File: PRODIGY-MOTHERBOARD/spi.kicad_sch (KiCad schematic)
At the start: 5 parts, among them U15 TXS0108EPW, U25 74HC138

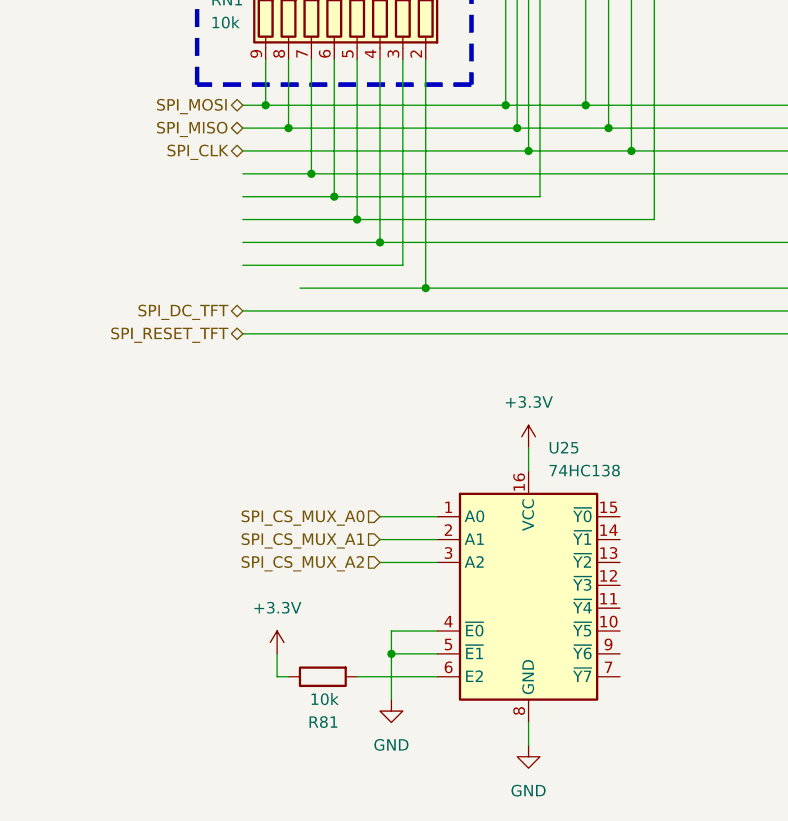
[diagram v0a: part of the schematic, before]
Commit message: Added proper debounce filter elements to buttons.
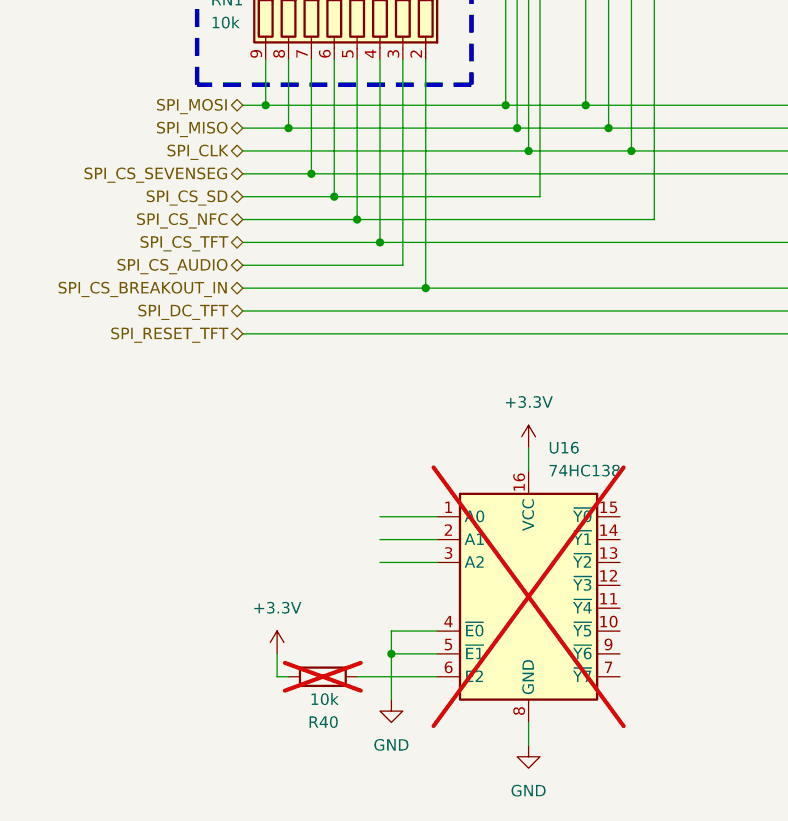
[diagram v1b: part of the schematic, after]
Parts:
- R40: renamed from R81; now not fitted
- U16: renamed from U25; now not fitted
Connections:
- net SPI_CS_SEVENSEG: now reaches RN1.7 (R6), U15.5 (A4)
- net SPI_CS_BREAKOUT_IN: now reaches RN1.2 (R1), U15.6 (A5)
- net SPI_CS_AUDIO: now reaches RN1.3 (R2)
- net CS_SD renamed SPI_CS_SD
- net NFC/SPI_CS_NFC renamed SPI_CS_NFC
- net SPI_CS_MUX_A0: no longer names the net of U16.1 (A0)
- net SPI_CS_MUX_A1: no longer names the net of U16.2 (A1)
- net SPI_CS_MUX_A2: no longer names the net of U16.3 (A2)
- net tft/SPI_CS_TFT renamed SPI_CS_TFT
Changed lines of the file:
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@@
 	(wire
 		(pts
-			(xy 40.64 110.49) (xy 54.61 110.49)
+			(xy 34.29 110.49) (xy 54.61 110.49)
 		)
 		(stroke
@@
 		)
 	)
-	(hierarchical_label "SPI_CS_MUX_A1"
-		(shape input)
-		(at 49.53 138.43 180)
+	(hierarchical_label "SPI_CS_TFT"
+		(shape bidirectional)
+		(at 34.29 105.41 180)
 		(fields_autoplaced yes)
 		(effects
@@
 		)
 	)
-	(hierarchical_label "SPI_CS_MUX_A0"
-		(shape input)
-		(at 49.53 135.89 180)
+	(hierarchical_label "SPI_CS_NFC"
+		(shape bidirectional)
+		(at 34.29 102.87 180)
+		(fields_autoplaced yes)
+		(effects
+			(font
+				(size 1.27 1.27)
+			)
+			(justify right)
+		)
+	)
+	(hierarchical_label "SPI_CS_SEVENSEG"
+		(shape bidirectional)
+		(at 34.29 97.79 180)
 		(fields_autoplaced yes)
 		(effects
@@
 		)
 	)
-	(hierarchical_label "SPI_CS_MUX_A2"
-		(shape input)
-		(at 49.53 140.97 180)
-		(fields_autoplaced yes)
-		(effects
-			(font
-				(size 1.27 1.27)
-			)
-			(justify right)
-		)
-	)
 	(hierarchical_label "SPI_MISO"
 		(shape bidirectional)
@@
 		)
 	)
+	(hierarchical_label "SPI_CS_SD"
+		(shape bidirectional)
+		(at 34.29 100.33 180)
+		(fields_autoplaced yes)
+		(effects
+			(font
+				(size 1.27 1.27)
+			)
+			(justify right)
+		)
+	)
 	(hierarchical_label "SPI_MOSI_BREAKOUT"
 		(shape bidirectional)
@@
 		(shape output)
 		(at 86.36 52.07 180)
+		(fields_autoplaced yes)
+		(effects
+			(font
+				(size 1.27 1.27)
+			)
+			(justify right)
+		)
+	)
+	(hierarchical_label "SPI_CS_BREAKOUT_IN"
+		(shape bidirectional)
+		(at 34.29 110.49 180)
+		(fields_autoplaced yes)
+		(effects
+			(font
+				(size 1.27 1.27)
+			)
+			(justify right)
+		)
+	)
+	(hierarchical_label "SPI_CS_AUDIO"
+		(shape bidirectional)
+		(at 34.29 107.95 180)
 		(fields_autoplaced yes)
 		(effects
@@
 		(dnp no)
 		(fields_autoplaced yes)
-		(property "Reference" "#PWR080"
+		(property "Reference" "#PWR092"
 			(at 171.45 83.82 0)
 			(effects
@@
 			(project "PRODIGY-MOTHERBOARD"
 				(path "/f1c25860-8989-4190-bd24-2491d23ca7d9/e2913798-f444-47a6-8b64-53020d7d816b"
-					(reference "#PWR080")
+					(reference "#PWR092")
 					(unit 1)
 				)
@@
 		(in_bom yes)
 		(on_board yes)
-		(dnp no)
-		(property "Reference" "R81"
+		(dnp yes)
+		(property "Reference" "R40"
 			(at 44.958 158.75 90)
 			(effects
@@
 			(project "PRODIGY-MOTHERBOARD"
 				(path "/f1c25860-8989-4190-bd24-2491d23ca7d9/e2913798-f444-47a6-8b64-53020d7d816b"
-					(reference "R81")
+					(reference "R40")
 					(unit 1)
 				)
@@
 		(dnp no)
 		(fields_autoplaced yes)
-		(property "Reference" "#PWR082"
+		(property "Reference" "#PWR090"
 			(at 176.53 78.74 0)
 			(effects
@@
 			(project "PRODIGY-MOTHERBOARD"
 				(path "/f1c25860-8989-4190-bd24-2491d23ca7d9/e2913798-f444-47a6-8b64-53020d7d816b"
-					(reference "#PWR082")
+					(reference "#PWR090")
 					(unit 1)
 				)
@@
 		(dnp no)
 		(fields_autoplaced yes)
-		(property "Reference" "#PWR0193"
+		(property "Reference" "#PWR094"
 			(at 66.04 132.08 0)
 			(effects
@@
 			(project "PRODIGY-MOTHERBOARD"
 				(path "/f1c25860-8989-4190-bd24-2491d23ca7d9/e2913798-f444-47a6-8b64-53020d7d816b"
-					(reference "#PWR0193")
+					(reference "#PWR094")
 					(unit 1)
 				)
@@
 		(dnp no)
 		(fields_autoplaced yes)
-		(property "Reference" "#PWR0195"
+		(property "Reference" "#PWR097"
 			(at 66.04 167.64 0)
 			(effects
@@
 			(project "PRODIGY-MOTHERBOARD"
 				(path "/f1c25860-8989-4190-bd24-2491d23ca7d9/e2913798-f444-47a6-8b64-53020d7d816b"
-					(reference "#PWR0195")
+					(reference "#PWR097")
 					(unit 1)
 				)
@@
 		(in_bom yes)
 		(on_board yes)
-		(dnp no)
-		(fields_autoplaced yes)
-		(property "Reference" "U25"
+		(dnp yes)
+		(fields_autoplaced yes)
+		(property "Reference" "U16"
 			(at 68.2341 128.27 0)
 			(effects
@@
 			(project "PRODIGY-MOTHERBOARD"
 				(path "/f1c25860-8989-4190-bd24-2491d23ca7d9/e2913798-f444-47a6-8b64-53020d7d816b"
-					(reference "U25")
+					(reference "U16")
 					(unit 1)
 				)
@@
 		(dnp no)
 		(fields_autoplaced yes)
-		(property "Reference" "#PWR079"
+		(property "Reference" "#PWR089"
 			(at 54.61 78.74 0)
 			(effects
@@
 			(project "PRODIGY-MOTHERBOARD"
 				(path "/f1c25860-8989-4190-bd24-2491d23ca7d9/e2913798-f444-47a6-8b64-53020d7d816b"
-					(reference "#PWR079")
+					(reference "#PWR089")
 					(unit 1)
 				)
@@
 		(dnp no)
 		(fields_autoplaced yes)
-		(property "Reference" "#PWR0192"
+		(property "Reference" "#PWR096"
 			(at 50.8 162.56 0)
 			(effects
@@
 			(project "PRODIGY-MOTHERBOARD"
 				(path "/f1c25860-8989-4190-bd24-2491d23ca7d9/e2913798-f444-47a6-8b64-53020d7d816b"
-					(reference "#PWR0192")
+					(reference "#PWR096")
 					(unit 1)
 				)
@@
 		(dnp no)
 		(fields_autoplaced yes)
-		(property "Reference" "#PWR081"
+		(property "Reference" "#PWR093"
 			(at 173.99 130.81 0)
 			(effects
@@
 			(project "PRODIGY-MOTHERBOARD"
 				(path "/f1c25860-8989-4190-bd24-2491d23ca7d9/e2913798-f444-47a6-8b64-53020d7d816b"
-					(reference "#PWR081")
+					(reference "#PWR093")
 					(unit 1)
 				)
@@
 		(dnp no)
 		(fields_autoplaced yes)
-		(property "Reference" "#PWR083"
+		(property "Reference" "#PWR091"
 			(at 194.31 78.74 0)
 			(effects
@@
 			(project "PRODIGY-MOTHERBOARD"
 				(path "/f1c25860-8989-4190-bd24-2491d23ca7d9/e2913798-f444-47a6-8b64-53020d7d816b"
-					(reference "#PWR083")
+					(reference "#PWR091")
 					(unit 1)
 				)
@@
 		(dnp no)
 		(fields_autoplaced yes)
-		(property "Reference" "#PWR0194"
+		(property "Reference" "#PWR095"
 			(at 38.1 154.94 0)
 			(effects
@@
 			(project "PRODIGY-MOTHERBOARD"
 				(path "/f1c25860-8989-4190-bd24-2491d23ca7d9/e2913798-f444-47a6-8b64-53020d7d816b"
-					(reference "#PWR0194")
+					(reference "#PWR095")
 					(unit 1)
 				)

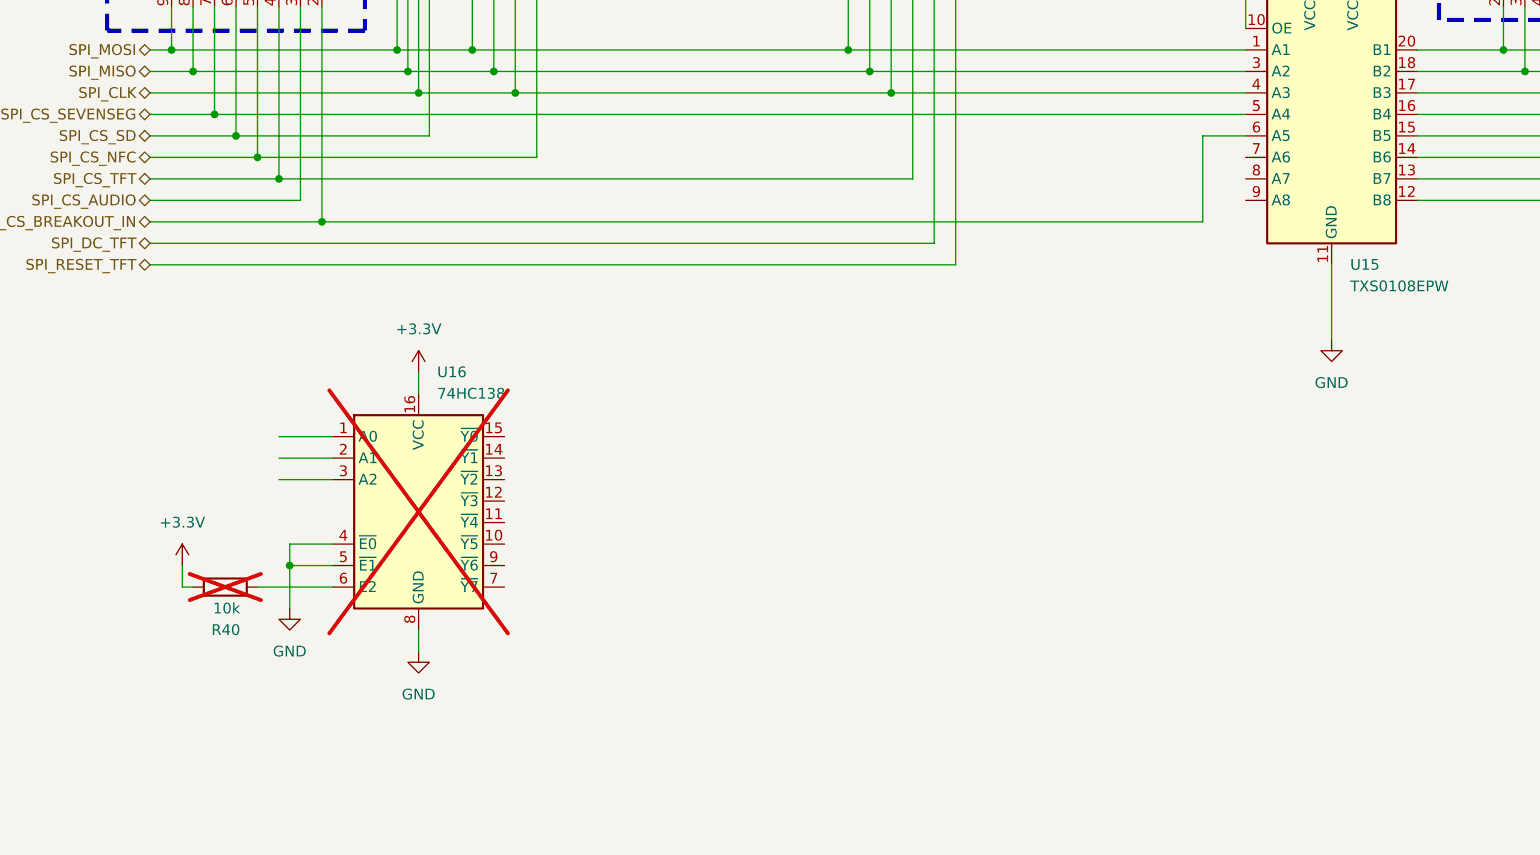
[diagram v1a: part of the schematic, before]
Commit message: Submitted V0 for evaluation. Avaiting feedback.
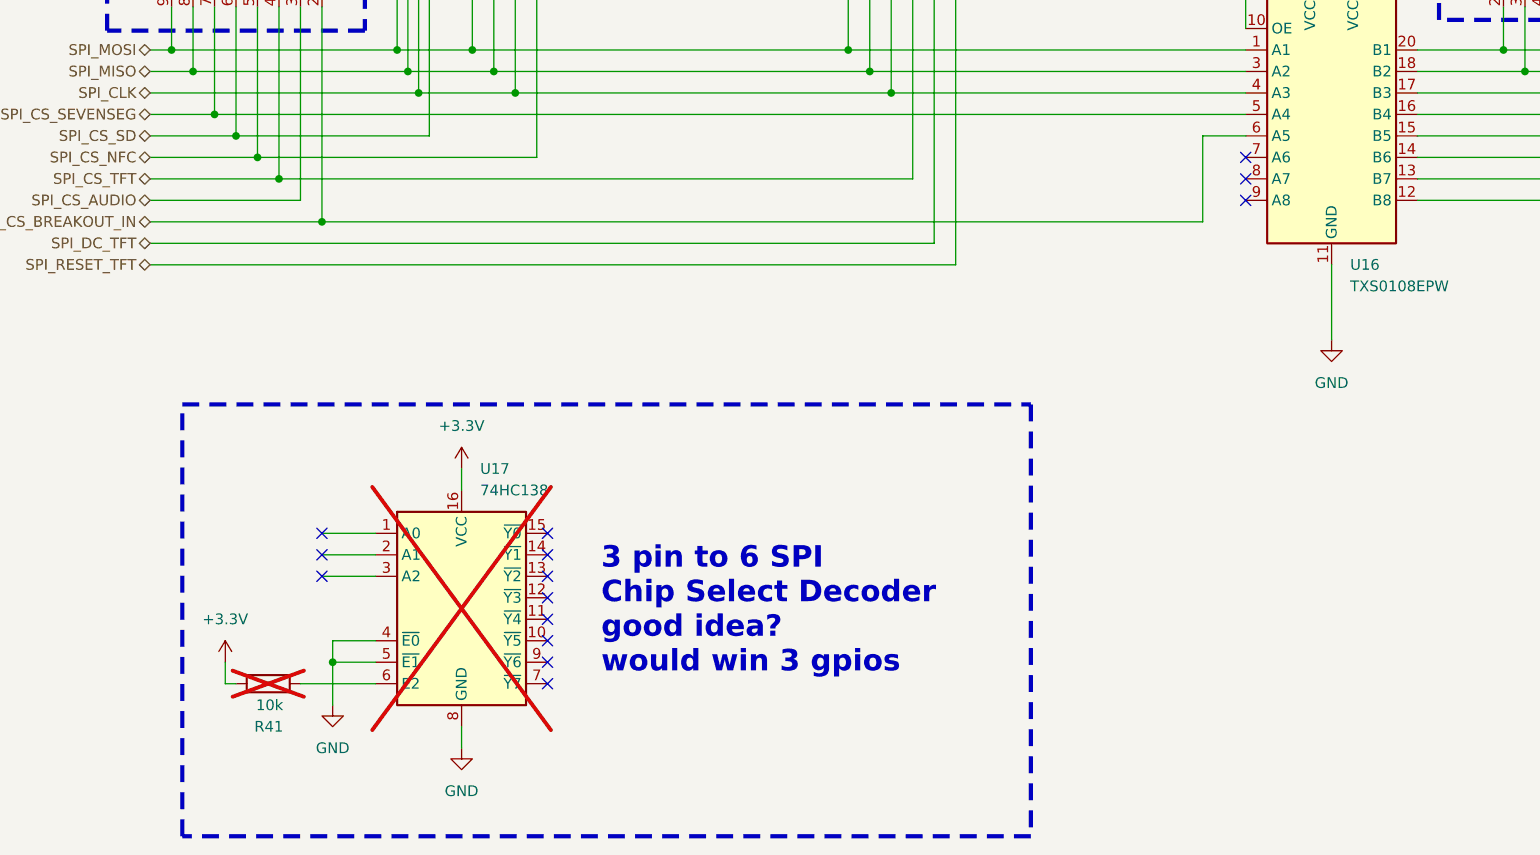
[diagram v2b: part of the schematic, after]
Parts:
- renumbered R40 to R41, U15 to U16, U16 to U17
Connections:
- no-connect marks 1 -> 15
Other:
- note added: "3 pin to 6 SPI Chip Select Decoder good idea? would win 3 gpios"
- moved on the sheet: R41, U17

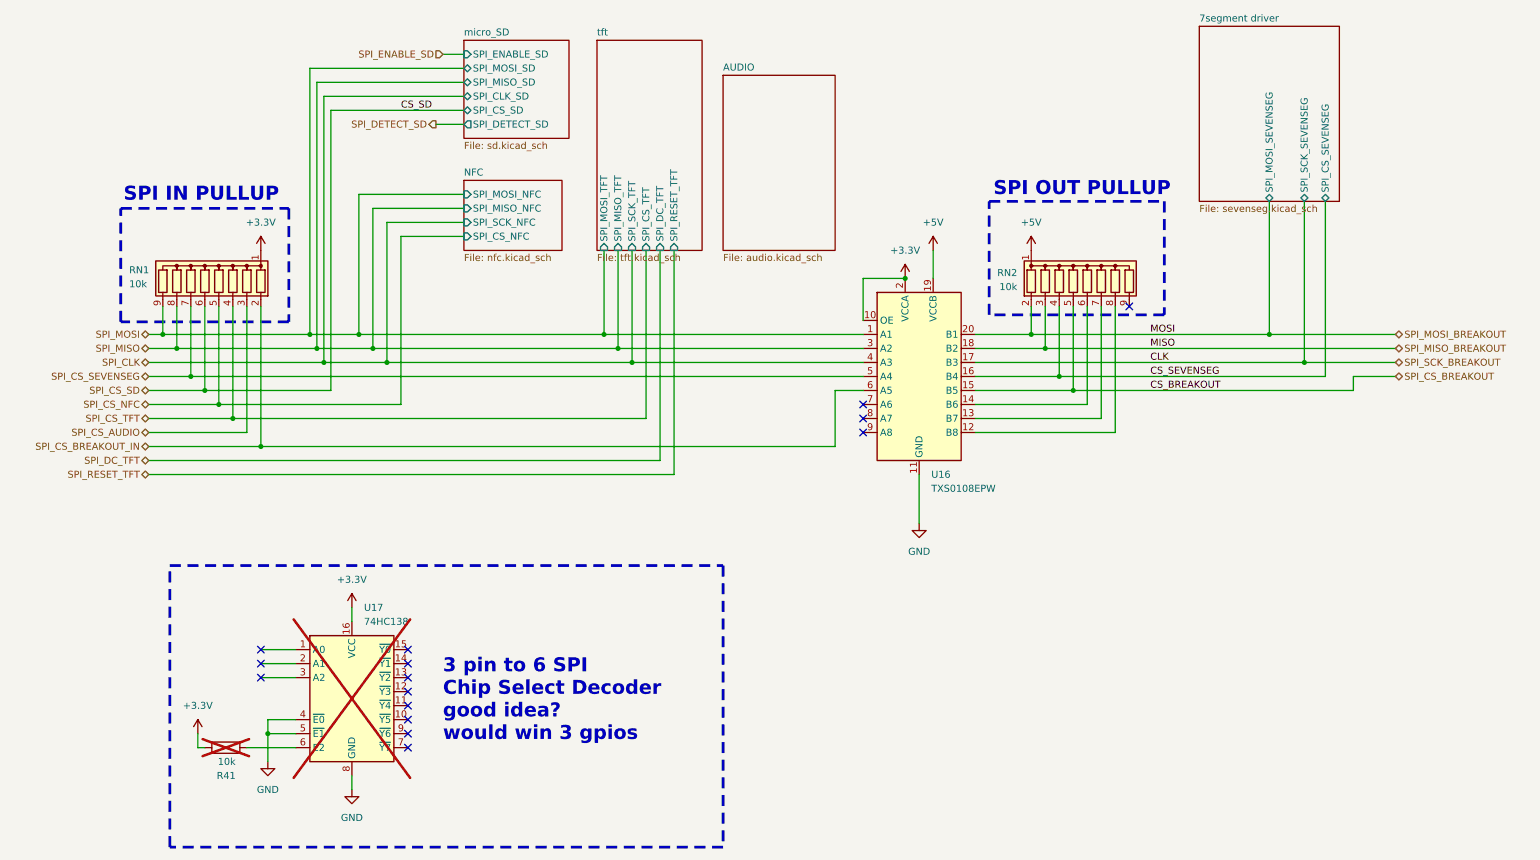
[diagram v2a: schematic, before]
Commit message: MCU schematic done. Started Analog design.
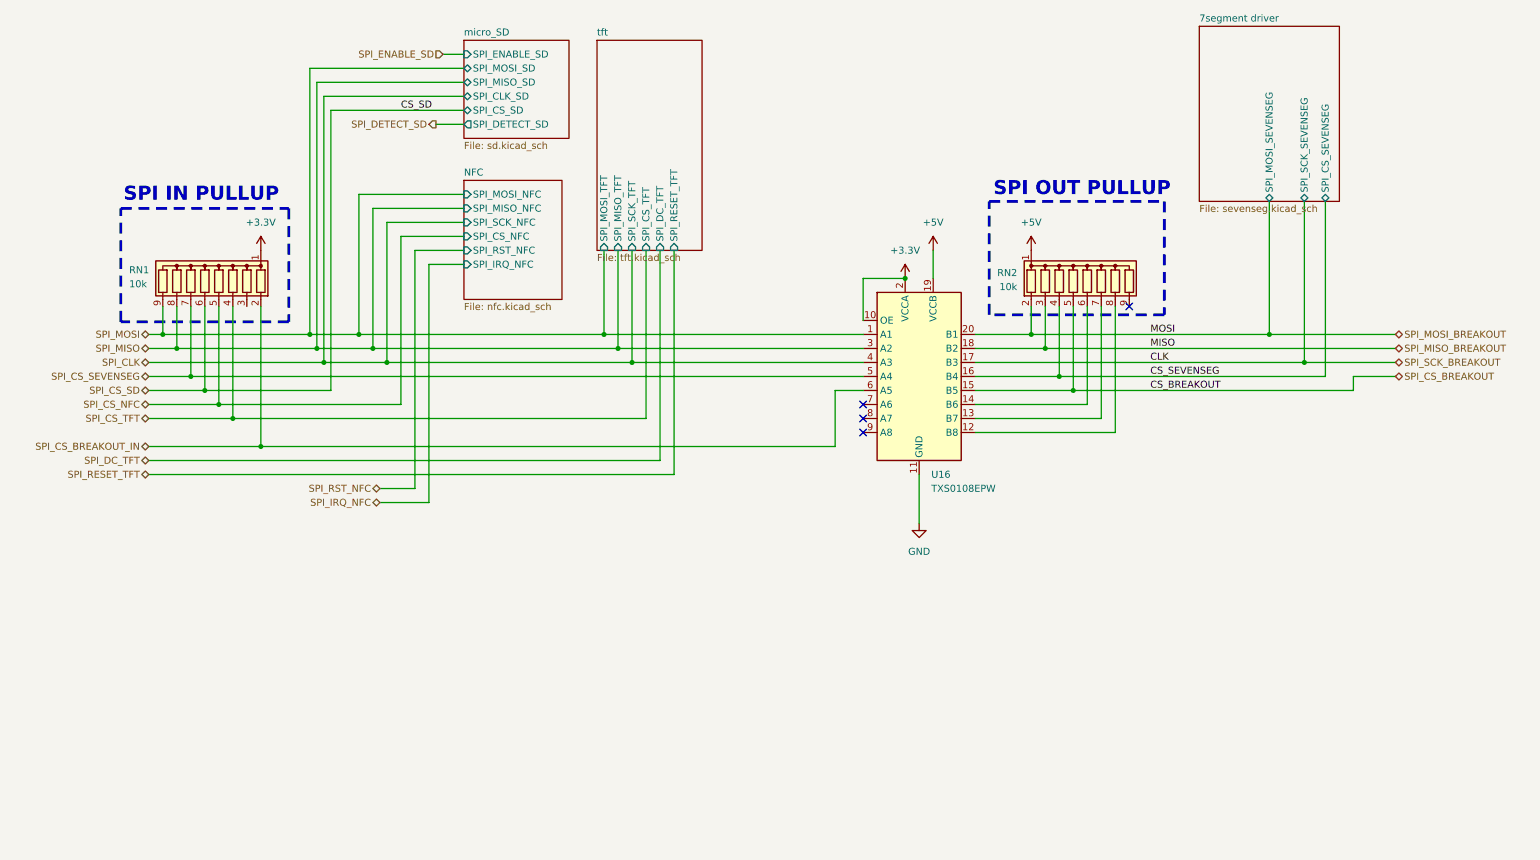
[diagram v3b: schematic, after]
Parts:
- removed R41: 10k, symbol Device:R
- removed U17: 74HC138, Package_SO:SOIC-16_3.9x9.9mm_P1.27mm, symbol 74xx:74HC138
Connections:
- net SPI_CS_AUDIO: no longer names the net of RN1.3 (R2)
- no-connect marks 15 -> 4
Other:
- removed sheet AUDIO
- sheet NFC ports: added SPI_IRQ_NFC, SPI_RST_NFC; removed none
- note removed: "3 pin to 6 SPI Chip Select Decoder good idea? would win 3 gpios"
